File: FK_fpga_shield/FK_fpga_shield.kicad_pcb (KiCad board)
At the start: 2 copper layers, 4 parts, among them J1 USB_B_Mini, J2 Conn_02x20_Odd_Even, J3 Conn_02x20_Odd_Even, U1 FT232RL

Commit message: change connector sym/footprint on fpgashield
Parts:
- added J4: molex-35363-0660, FK_fpga_shield_custom_footprints:molex-35363-0660, F.Cu at (33.8, 25.5)
- added J5: molex-35363-0660, FK_fpga_shield_custom_footprints:molex-35363-0660, F.Cu at (45.5, 25.5)
- added J6: molex-35363-0660, FK_fpga_shield_custom_footprints:molex-35363-0660, F.Cu at (57.3, 25.5)
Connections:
- J2 pad 11: /5V -> GND
- J3 pad 11: /5V -> GND
- U1 pad 20: Net-(U1-Pad20) -> GND

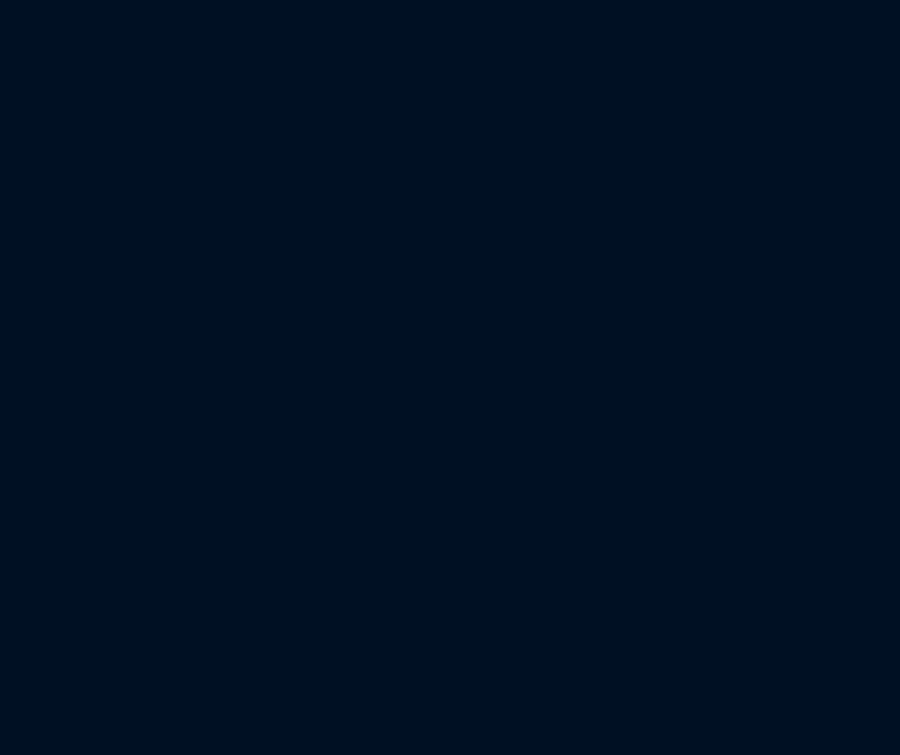
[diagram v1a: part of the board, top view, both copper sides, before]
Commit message: change connector to microclasp 4 wire
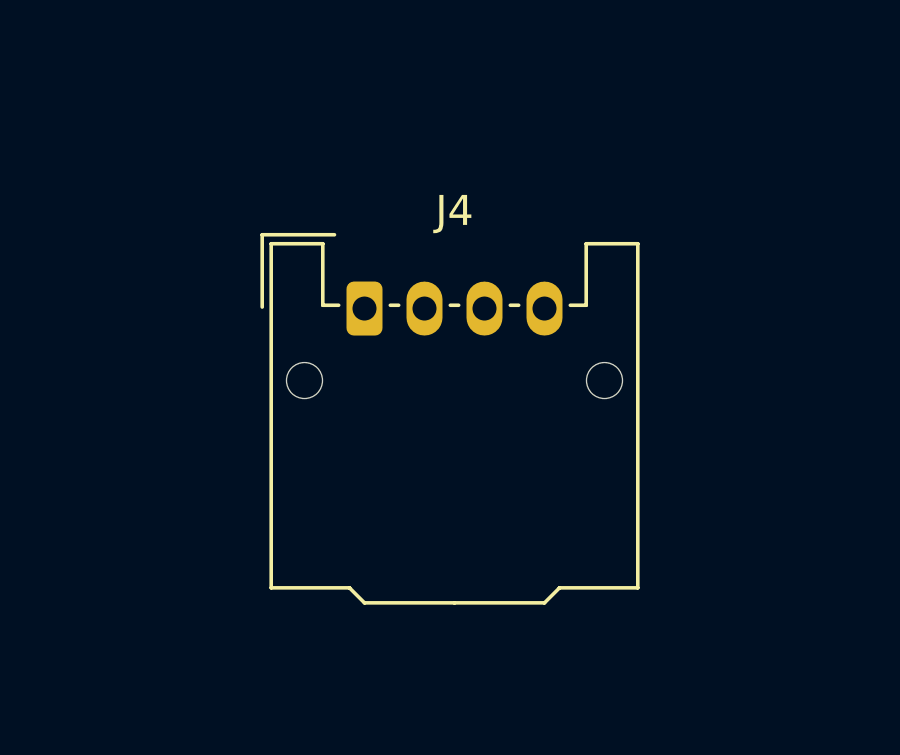
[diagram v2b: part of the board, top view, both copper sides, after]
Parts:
- added J4: molex-51382-0400-microclasp, FK_fpga_shield_custom_footprints:Molex_MicroClasp_55935-0410_1x04_P2.00mm_Horizontal_3DMODEL, F.Cu at (85.2, 58.5)
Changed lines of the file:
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@@
     (tracks 0)
     (zones 0)
-    (modules 7)
+    (modules 8)
     (nets 108)
   )
@@
     (add_net "Net-(U1-Pad9)")
   )
+  (module FK_fpga_shield_custom_footprints:Molex_MicroClasp_55935-0410_1x04_P2.00mm_Horizontal_3DMODEL (layer F.Cu)
+    (at 85.25 58.5)
+    (descr "Molex MicroClasp Wire-to-Board System, 55935-0410, with PCB locator, 4 Pins (http://www.molex.com/pdm_docs/sd/559350210_sd.pdf), generated with kicad-footprint-generator")
+    (tags "connector Molex MicroClasp horizontal")
+    (fp_text reference J4 (at 3 -3.25) (layer F.SilkS)
+      (effects (font (size 1 1) (thickness 0.15)))
+    )
+    (fp_text value molex-51382-0400-microclasp (at 3 10.9) (layer F.Fab)
+      (effects (font (size 1 1) (thickness 0.15)))
+    )
+    (fp_text user %R (at 3 8.5) (layer F.Fab)
+      (effects (font (size 1 1) (thickness 0.15)))
+    )
+    (fp_line (start 9.5 -2.55) (end -3.5 -2.55) (layer F.CrtYd) (width 0.05))
+    (fp_line (start 9.5 10.2) (end 9.5 -2.55) (layer F.CrtYd) (width 0.05))
+    (fp_line (start -3.5 10.2) (end 9.5 10.2) (layer F.CrtYd) (width 0.05))
+    (fp_line (start -3.5 -2.55) (end -3.5 10.2) (layer F.CrtYd) (width 0.05))
+    (fp_line (start 0 0.707107) (end 0.5 0) (layer F.Fab) (width 0.1))
+    (fp_line (start -0.5 0) (end 0 0.707107) (layer F.Fab) (width 0.1))
+    (fp_line (start -3.41 -2.46) (end -1 -2.46) (layer F.SilkS) (width 0.12))
+    (fp_line (start -3.41 -0.05) (end -3.41 -2.46) (layer F.SilkS) (width 0.12))
+    (fp_line (start 4.86 -0.11) (end 5.14 -0.11) (layer F.SilkS) (width 0.12))
+    (fp_line (start 2.86 -0.11) (end 3.14 -0.11) (layer F.SilkS) (width 0.12))
+    (fp_line (start 0.86 -0.11) (end 1.14 -0.11) (layer F.SilkS) (width 0.12))
+    (fp_line (start 7.39 -0.11) (end 6.86 -0.11) (layer F.SilkS) (width 0.12))
+    (fp_line (start 7.39 -2.16) (end 7.39 -0.11) (layer F.SilkS) (width 0.12))
+    (fp_line (start 9.11 -2.16) (end 7.39 -2.16) (layer F.SilkS) (width 0.12))
+    (fp_line (start 9.11 9.31) (end 9.11 -2.16) (layer F.SilkS) (width 0.12))
+    (fp_line (start 6.5 9.31) (end 9.11 9.31) (layer F.SilkS) (width 0.12))
+    (fp_line (start 6 9.81) (end 6.5 9.31) (layer F.SilkS) (width 0.12))
+    (fp_line (start 3 9.81) (end 6 9.81) (layer F.SilkS) (width 0.12))
+    (fp_line (start -1.39 -0.11) (end -0.86 -0.11) (layer F.SilkS) (width 0.12))
+    (fp_line (start -1.39 -2.16) (end -1.39 -0.11) (layer F.SilkS) (width 0.12))
+    (fp_line (start -3.11 -2.16) (end -1.39 -2.16) (layer F.SilkS) (width 0.12))
+    (fp_line (start -3.11 9.31) (end -3.11 -2.16) (layer F.SilkS) (width 0.12))
+    (fp_line (start -0.5 9.31) (end -3.11 9.31) (layer F.SilkS) (width 0.12))
+    (fp_line (start 0 9.81) (end -0.5 9.31) (layer F.SilkS) (width 0.12))
+    (fp_line (start 3 9.81) (end 0 9.81) (layer F.SilkS) (width 0.12))
+    (fp_line (start 7.5 0) (end 3 0) (layer F.Fab) (width 0.1))
+    (fp_line (start 7.5 -2.05) (end 7.5 0) (layer F.Fab) (width 0.1))
+    (fp_line (start 9 -2.05) (end 7.5 -2.05) (layer F.Fab) (width 0.1))
+    (fp_line (start 9 9.2) (end 9 -2.05) (layer F.Fab) (width 0.1))
+    (fp_line (start 6.39 9.2) (end 9 9.2) (layer F.Fab) (width 0.1))
+    (fp_line (start 5.89 9.7) (end 6.39 9.2) (layer F.Fab) (width 0.1))
+    (fp_line (start 3 9.7) (end 5.89 9.7) (layer F.Fab) (width 0.1))
+    (fp_line (start -1.5 0) (end 3 0) (layer F.Fab) (width 0.1))
+    (fp_line (start -1.5 -2.05) (end -1.5 0) (layer F.Fab) (width 0.1))
+    (fp_line (start -3 -2.05) (end -1.5 -2.05) (layer F.Fab) (width 0.1))
+    (fp_line (start -3 9.2) (end -3 -2.05) (layer F.Fab) (width 0.1))
+    (fp_line (start -0.39 9.2) (end -3 9.2) (layer F.Fab) (width 0.1))
+    (fp_line (start 0.11 9.7) (end -0.39 9.2) (layer F.Fab) (width 0.1))
+    (fp_line (start 3 9.7) (end 0.11 9.7) (layer F.Fab) (width 0.1))
+    (pad "" np_thru_hole circle (at -2 2.4) (size 1.2 1.2) (drill 1.2) (layers *.Cu *.Mask))
+    (pad "" np_thru_hole circle (at 8 2.4) (size 1.2 1.2) (drill 1.2) (layers *.Cu *.Mask))
+    (pad 4 thru_hole oval (at 6 0) (size 1.2 1.8) (drill 0.8) (layers *.Cu *.Mask)
+      (net 95 "Net-(J4-Pad4)"))
+    (pad 3 thru_hole oval (at 4 0) (size 1.2 1.8) (drill 0.8) (layers *.Cu *.Mask)
+      (net 98 "Net-(J4-Pad3)"))
+    (pad 2 thru_hole oval (at 2 0) (size 1.2 1.8) (drill 0.8) (layers *.Cu *.Mask)
+      (net 97 "Net-(J4-Pad2)"))
+    (pad 1 thru_hole roundrect (at 0 0) (size 1.2 1.8) (drill 0.8) (layers *.Cu *.Mask) (roundrect_rratio 0.208333)
+      (net 96 "Net-(J4-Pad1)"))
+    (model ${KIPRJMOD}/559350430.stp
+      (offset (xyz 3 2 0))
+      (scale (xyz 1 1 1))
+      (rotate (xyz 180 0 0))
+    )
+  )
   (module FK_fpga_shield_custom_footprints:molex-35363-0660 (layer F.Cu)
     (at 57.29 25.5)
@@
     (fp_text value molex-35363-0660 (at 3.1 12) (layer F.Fab)
       (effects (font (size 1 1) (thickness 0.15)))
-    )
-    (fp_text user %R (at 2.25 5 90) (layer F.Fab)
-      (effects (font (size 0.9 0.9) (thickness 0.135)))
     )
     (fp_line (start 0.05 11) (end 0.05 -1) (layer F.SilkS) (width 0.12))
@@
     (fp_line (start 7.7 11.5) (end 7.7 -1.5) (layer F.CrtYd) (width 0.05))
     (fp_line (start 7.7 -1.5) (end -1.5 -1.5) (layer F.CrtYd) (width 0.05))
+    (fp_text user %R (at 2.25 5 90) (layer F.Fab)
+      (effects (font (size 0.9 0.9) (thickness 0.135)))
+    )
     (pad 4 thru_hole rect (at 0 0) (size 1.35 1.35) (drill 0.8) (layers *.Cu *.Mask)
       (net 103 "Net-(J6-Pad4)"))
@@
     (fp_text value molex-35363-0660 (at 3.1 12) (layer F.Fab)
       (effects (font (size 1 1) (thickness 0.15)))
-    )
-    (fp_text user %R (at 2.25 5 90) (layer F.Fab)
-      (effects (font (size 0.9 0.9) (thickness 0.135)))
     )
     (fp_line (start 0.05 11) (end 0.05 -1) (layer F.SilkS) (width 0.12))
@@
     (fp_line (start 7.7 11.5) (end 7.7 -1.5) (layer F.CrtYd) (width 0.05))
     (fp_line (start 7.7 -1.5) (end -1.5 -1.5) (layer F.CrtYd) (width 0.05))
+    (fp_text user %R (at 2.25 5 90) (layer F.Fab)
+      (effects (font (size 0.9 0.9) (thickness 0.135)))
+    )
     (pad 4 thru_hole rect (at 0 0) (size 1.35 1.35) (drill 0.8) (layers *.Cu *.Mask)
       (net 99 "Net-(J5-Pad4)"))
@@
     (fp_text value molex-35363-0660 (at 3.1 12) (layer F.Fab)
       (effects (font (size 1 1) (thickness 0.15)))
-    )
-    (fp_text user %R (at 2.25 5 90) (layer F.Fab)
-      (effects (font (size 0.9 0.9) (thickness 0.135)))
     )
     (fp_line (start 0.05 11) (end 0.05 -1) (layer F.SilkS) (width 0.12))
@@
     (fp_line (start 7.7 11.5) (end 7.7 -1.5) (layer F.CrtYd) (width 0.05))
     (fp_line (start 7.7 -1.5) (end -1.5 -1.5) (layer F.CrtYd) (width 0.05))
+    (fp_text user %R (at 2.25 5 90) (layer F.Fab)
+      (effects (font (size 0.9 0.9) (thickness 0.135)))
+    )
     (pad 4 thru_hole rect (at 0 0) (size 1.35 1.35) (drill 0.8) (layers *.Cu *.Mask)
       (net 95 "Net-(J4-Pad4)"))
